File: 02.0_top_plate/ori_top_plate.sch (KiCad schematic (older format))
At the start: 65 parts, among them U1 HOLE, U10 HOLE, U11 HOLE, U12 HOLE, U13 HOLE, U14 HOLE, U15 HOLE, U16 HOLE, U17 HOLE, U18 HOLE, U19 HOLE, U2 HOLE, U20 HOLE, U21 HOLE, U22 HOLE, U23 HOLE, U24 HOLE, U25 HOLE, U26 HOLE, U27 HOLE, U28 HOLE, U29 HOLE, U3 HOLE, U30 HOLE, U31 HOLE, U32 HOLE, U33 HOLE, U34 HOLE, U35 HOLE, U36 HOLE, U37 HOLE, U38 HOLE, U39 HOLE, U4 HOLE, U40 HOLE, U41 HOLE, U42 HOLE, U43 HOLE, U44 HOLE, U45 HOLE, U46 HOLE, U47 HOLE, U48 HOLE, U49 HOLE, U5 HOLE, U53 HOLE, U57 HOLE, U6 HOLE, U61 HOLE, U7 HOLE, U8 HOLE, U9 HOLE

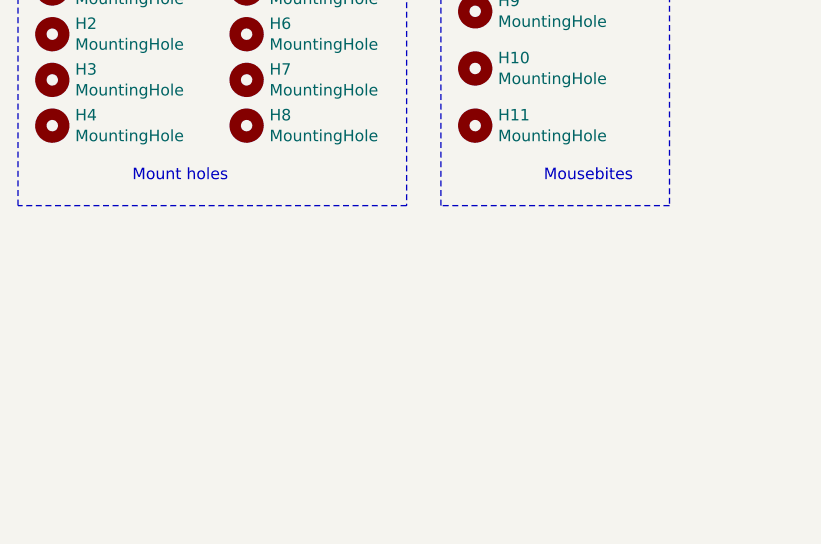
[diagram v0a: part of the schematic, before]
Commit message: modify top plate
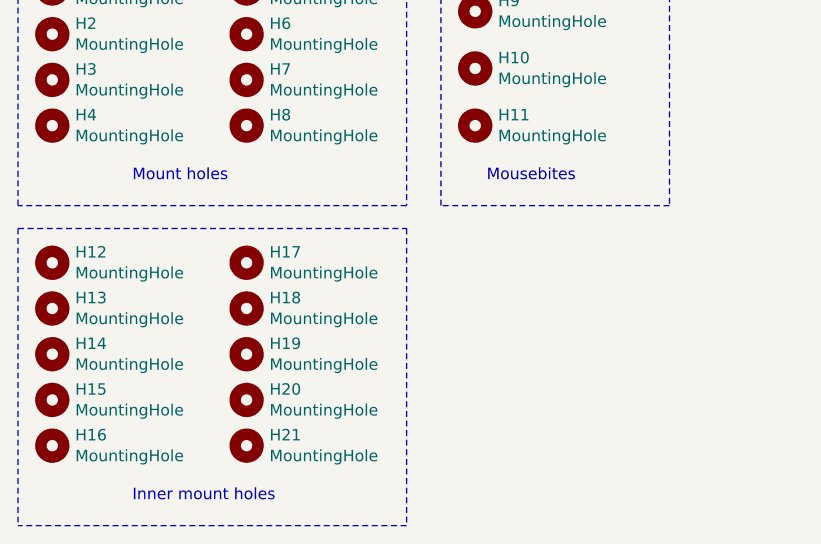
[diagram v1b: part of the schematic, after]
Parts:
- added H12, H13, H14, H15, H16, H17, H18, H19, H20, H21: MountingHole, MountingHole:MountingHole_2.2mm_M2, symbol Mechanical:MountingHole
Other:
- note added: "Inner mount holes"
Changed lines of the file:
@@
 	1    0    0    -1
 $EndComp
-Text Notes 4650 4250 0    50   ~ 0
+Text Notes 4400 4250 0    50   ~ 0
 Mousebites
 Wire Notes Line
@@
 Wire Notes Line
 	2350 4350 2350 3250
+$Comp
+L Mechanical:MountingHole H12
+U 1 1 611EB2C1
+P 2500 4600
+F 0 "H12" H 2600 4646 50  0000 L CNN
+F 1 "MountingHole" H 2600 4555 50  0000 L CNN
+F 2 "MountingHole:MountingHole_2.2mm_M2" H 2500 4600 50  0001 C CNN
+F 3 "~" H 2500 4600 50  0001 C CNN
+	1    2500 4600
+	1    0    0    -1
+$EndComp
+$Comp
+L Mechanical:MountingHole H13
+U 1 1 611EB2C7
+P 2500 4800
+F 0 "H13" H 2600 4846 50  0000 L CNN
+F 1 "MountingHole" H 2600 4755 50  0000 L CNN
+F 2 "MountingHole:MountingHole_2.2mm_M2" H 2500 4800 50  0001 C CNN
+F 3 "~" H 2500 4800 50  0001 C CNN
+	1    2500 4800
+	1    0    0    -1
+$EndComp
+$Comp
+L Mechanical:MountingHole H14
+U 1 1 611EB2CD
+P 2500 5000
+F 0 "H14" H 2600 5046 50  0000 L CNN
+F 1 "MountingHole" H 2600 4955 50  0000 L CNN
+F 2 "MountingHole:MountingHole_2.2mm_M2" H 2500 5000 50  0001 C CNN
+F 3 "~" H 2500 5000 50  0001 C CNN
+	1    2500 5000
+	1    0    0    -1
+$EndComp
+$Comp
+L Mechanical:MountingHole H15
+U 1 1 611EB2D3
+P 2500 5200
+F 0 "H15" H 2600 5246 50  0000 L CNN
+F 1 "MountingHole" H 2600 5155 50  0000 L CNN
+F 2 "MountingHole:MountingHole_2.2mm_M2" H 2500 5200 50  0001 C CNN
+F 3 "~" H 2500 5200 50  0001 C CNN
+	1    2500 5200
+	1    0    0    -1
+$EndComp
+$Comp
+L Mechanical:MountingHole H16
+U 1 1 611EB2D9
+P 2500 5400
+F 0 "H16" H 2600 5446 50  0000 L CNN
+F 1 "MountingHole" H 2600 5355 50  0000 L CNN
+F 2 "MountingHole:MountingHole_2.2mm_M2" H 2500 5400 50  0001 C CNN
+F 3 "~" H 2500 5400 50  0001 C CNN
+	1    2500 5400
+	1    0    0    -1
+$EndComp
+$Comp
+L Mechanical:MountingHole H17
+U 1 1 611EB2DF
+P 3350 4600
+F 0 "H17" H 3450 4646 50  0000 L CNN
+F 1 "MountingHole" H 3450 4555 50  0000 L CNN
+F 2 "MountingHole:MountingHole_2.2mm_M2" H 3350 4600 50  0001 C CNN
+F 3 "~" H 3350 4600 50  0001 C CNN
+	1    3350 4600
+	1    0    0    -1
+$EndComp
+$Comp
+L Mechanical:MountingHole H18
+U 1 1 611EB2E5
+P 3350 4800
+F 0 "H18" H 3450 4846 50  0000 L CNN
+F 1 "MountingHole" H 3450 4755 50  0000 L CNN
+F 2 "MountingHole:MountingHole_2.2mm_M2" H 3350 4800 50  0001 C CNN
+F 3 "~" H 3350 4800 50  0001 C CNN
+	1    3350 4800
+	1    0    0    -1
+$EndComp
+$Comp
+L Mechanical:MountingHole H19
+U 1 1 611EB2EB
+P 3350 5000
+F 0 "H19" H 3450 5046 50  0000 L CNN
+F 1 "MountingHole" H 3450 4955 50  0000 L CNN
+F 2 "MountingHole:MountingHole_2.2mm_M2" H 3350 5000 50  0001 C CNN
+F 3 "~" H 3350 5000 50  0001 C CNN
+	1    3350 5000
+	1    0    0    -1
+$EndComp
+Text Notes 2850 5650 0    50   ~ 0
+Inner mount holes
+Wire Notes Line
+	4050 5750 2350 5750
+$Comp
+L Mechanical:MountingHole H20
+U 1 1 611F35FE
+P 3350 5200
+F 0 "H20" H 3450 5246 50  0000 L CNN
+F 1 "MountingHole" H 3450 5155 50  0000 L CNN
+F 2 "MountingHole:MountingHole_2.2mm_M2" H 3350 5200 50  0001 C CNN
+F 3 "~" H 3350 5200 50  0001 C CNN
+	1    3350 5200
+	1    0    0    -1
+$EndComp
+$Comp
+L Mechanical:MountingHole H21
+U 1 1 611F3604
+P 3350 5400
+F 0 "H21" H 3450 5446 50  0000 L CNN
+F 1 "MountingHole" H 3450 5355 50  0000 L CNN
+F 2 "MountingHole:MountingHole_2.2mm_M2" H 3350 5400 50  0001 C CNN
+F 3 "~" H 3350 5400 50  0001 C CNN
+	1    3350 5400
+	1    0    0    -1
+$EndComp
+Wire Notes Line
+	2350 4450 4050 4450
+Wire Notes Line
+	4050 4450 4050 5750
+Wire Notes Line
+	2350 4450 2350 5750
 $EndSCHEMATC
